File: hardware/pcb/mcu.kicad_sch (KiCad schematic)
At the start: 108 parts, among them J1 Conn_02x03_Odd_Even, J12 Conn_01x05_Pin, J3 TPS43_FPC, J6 AudioJack4, SW1 SW_PUSH, SW10 SW_PUSH, SW12 SW_PUSH, SW14 SW_PUSH, SW15 SW_PUSH, SW17 SW_PUSH, SW19 SW_PUSH, SW21 SW_PUSH, SW24 SW_PUSH, SW26 SW_PUSH, SW27 SW_PUSH, SW3 SW_PUSH, SW30 SW_PUSH, SW31 SW_PUSH, SW33 SW_PUSH, SW35 SW_PUSH, SW38 SW_PUSH, SW40 SW_PUSH, SW41 SW_PUSH, SW43 SW_PUSH, SW45 SW_PUSH, SW47 SW_PUSH, SW49 SW_PUSH, SW5 SW_PUSH, SW52 SW_PUSH, SW8 SW_PUSH, U12 SiP32431DR3, U2 D, U3 D, U6 ESP32-S3-WROOM-1, U8 NRF24L01_Breakout, U9 SRV05-4

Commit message: élagage des feuilles + réparation des tables de bibliothèques
Mae a élagué dans l'éditeur :
- mcu  : 108 -> 16 composants. Restent le S3, le nRF24, leurs découplages, le
  connecteur de prog et les 100 ohms. Partis : la matrice 26 switchs / 24
  diodes, les 11 TVS, le TRRS, l'écran, le trackpad.
- usbc : 6 -> 4 composants. Le hub CH334R (U53) est parti, il venait du coffre
  P4 et n'avait rien à faire dans une souris. Restent J48, U54 (USBLC6) et les
  deux 5k1 de CC.

Tables de bibliothèques réparées : elles pointaient vers des fichiers absents ou
renommés (optical mouse.lib -> optical_mouse.lib, nice_nano, RP2040, SSD1306).
Mouse.pretty rapatrié du fork : les 6 empreintes de la coque en dépendent.

ERC : 96 -> 24 violations.

Co-Authored-By: Claude Opus 5 <noreply@anthropic.com>
Claude-Session: https://claude.ai/code/session_01GfX5RmekmQi78Dm37qsT4Z
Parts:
- removed C5, C6: 100nF, Capacitor_SMD:C_0603_1608Metric_Pad1.08x0.95mm_HandSolder, symbol Device:C
- removed C9: 1uF, Capacitor_SMD:C_0805_2012Metric_Pad1.18x1.45mm_HandSolder, symbol Device:C
- removed D100, D101, D102, D103, D104, D105, D106, D107, D108, D109, D110: SD05C-01F, Diode_SMD:D_SOD-323, symbol Diode:SD05C-01F
- removed D11, D13, D16, D18, D2, D20, D21, D24, D26, D28, D3, D30, D32, D33, D36, D38, D40, D41, D43, D46, D48, D6, D8, D9, U2, U3: D, Diode_SMD:D_SOD-123, symbol Device:D
- removed H5, H6, H7, H8: MountingHole_Pad_MP, MountingHole:MountingHole_3.2mm_M3_DIN965_Pad, symbol Mechanical:MountingHole_Pad_MP
- removed J12: Conn_01x05_Pin, Connector_PinHeader_2.54mm:PinHeader_1x05_P2.54mm_Vertical, symbol Connector:Conn_01x05_Pin
- removed J3: TPS43_FPC, Connector_FFC-FPC:Hirose_FH12-6S-0.5SH_1x06-1MP_P0.50mm_Horizontal, symbol Connector_Generic:Conn_01x06
- removed J6: AudioJack4, EKR82-footprint:MJ-4PP-9_rev3, symbol Connector_Audio:AudioJack4
- removed R11, R14, R20, R21, R23, R25, R27, R4, R45, R47, R6, R7, R9: 100, Resistor_SMD:R_0603_1608Metric_Pad0.98x0.95mm_HandSolder, symbol Device:R
- removed R29, R32: 4.7k, Resistor_SMD:R_0603_1608Metric_Pad0.98x0.95mm_HandSolder, symbol Device:R
- removed R35, R42: 100k, Resistor_SMD:R_0603_1608Metric_Pad0.98x0.95mm_HandSolder, symbol Device:R
- removed SW1, SW10, SW12, SW14, SW15, SW17, SW19, SW21, SW24, SW26, SW27, SW3, SW30, SW31, SW33, SW35, SW38, SW40, SW41, SW43, SW45, SW47, SW49, SW5, SW52, SW8: SW_PUSH, key:SW_Cherry_MX_1.00u_PCB, symbol corne-cherry-rescue:SW_PUSH-kbd-corne-cherry-rescue
- removed U12: SiP32431DR3, Package_TO_SOT_SMD:SOT-363_SC-70-6, symbol Power_Management:SiP32431DR3
- removed U9: SRV05-4, Package_TO_SOT_SMD:SOT-23-6, symbol Power_Protection:SRV05-4
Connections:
- no-connect marks 5 -> 4

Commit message: feuille sensor + correction de mon analyse de la radio
La liaison S3 <-> nRF24 est intacte : je l'avais lue comme cassée alors que
chaque ligne passe par sa résistance série de 100 ohms, nommée localement d'un
côté (SCK_L / MOSI_L / MISO_L) et anonyme de l'autre. Rien à réparer :
  U8.5 SCK  -R30- U6.31 (GPIO38)   U8.4 CSN -R36- U6.9  (GPIO16)
  U8.6 MOSI -R18- U6.33 (GPIO40)   U8.3 CE  -R39- U6.8  (GPIO15)
  U8.7 MISO -R16- U6.32 (GPIO39)   U8.8 IRQ -R41- U6.34 (GPIO41)

Ajout de sensor.kicad_sch, cinquième feuille de la hiérarchie, avec la liste de
ce qui doit y être posé et les références exactes à respecter — SW1/SW2/SW3,
LD1/LQ1, U2 — pour que le F8 retrouve les empreintes verrouillées du PCB.

Les 20 GPIO libérés par le retrait de la matrice apparaissent maintenant en
pin_not_connected : c'est attendu, ils attendent le câblage du capteur.

Note : j'ai tenté de poser le PWR_FLAG du +5V par script, sans succès — le
symbole n'atterrissait pas sur le net. Revert. À poser dans l'éditeur.

Co-Authored-By: Claude Opus 5 <noreply@anthropic.com>
Claude-Session: https://claude.ai/code/session_01GfX5RmekmQi78Dm37qsT4Z
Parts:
- removed R49: 10k, Resistor_SMD:R_0603_1608Metric_Pad0.98x0.95mm_HandSolder, symbol Device:R
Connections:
- net CS_DPL: no longer names the net of U6.22 (GPIO14/TOUCH14/ADC2_CH3/FSPIWP/FSPIDQS/SUBSPIWP)
- net CS_P4: no longer names the net of U6.15 (GPIO3/TOUCH3/ADC1_CH2)
- net IRQ_P4: no longer names the net of U6.16 (GPIO46)
- net LINK_5V_EN: no longer names the net of U6.23 (GPIO21)
- net LINK_RX: no longer names the net of U6.11 (GPIO18/U1RXD/ADC2_CH7/CLK_OUT3)
- net LINK_TX: no longer names the net of U6.10 (GPIO17/U1TXD/ADC2_CH6)
- net TP_RDY: no longer names the net of U6.35 (MTMS/GPIO42)
- net TP_SCL: no longer names the net of U6.25 (GPIO48/SPICLK_N/SUBSPICLK_N_DIFF)
- net TP_SDA: no longer names the net of U6.24 (GPIO47/SPICLK_P/SUBSPICLK_P_DIFF)
- net col0: no longer names the net of U6.4 (GPIO4/TOUCH4/ADC1_CH3)
- net col1: no longer names the net of U6.5 (GPIO5/TOUCH5/ADC1_CH4)
- net col2: no longer names the net of U6.7 (GPIO7/TOUCH7/ADC1_CH6)
- net col3: no longer names the net of U6.17 (GPIO9/TOUCH9/ADC1_CH8/FSPIHD/SUBSPIHD)
- net col4: no longer names the net of U6.18 (GPIO10/TOUCH10/ADC1_CH9/FSPICS0/FSPIIO4/SUBSPICS0)
- net col5: no longer names the net of U6.19 (GPIO11/TOUCH11/ADC2_CH0/FSPID/FSPIIO5/SUBSPID)
- net col6: no longer names the net of U6.20 (GPIO12/TOUCH12/ADC2_CH1/FSPICLK/FSPIIO6/SUBSPICLK)
- net row0: no longer names the net of U6.39 (GPIO1/TOUCH1/ADC1_CH0)
- net row1: no longer names the net of U6.38 (GPIO2/TOUCH2/ADC1_CH1)
- net row2: no longer names the net of U6.12 (GPIO8/TOUCH8/ADC1_CH7/SUBSPICS1)
- net row3: no longer names the net of U6.6 (GPIO6/TOUCH6/ADC1_CH5)

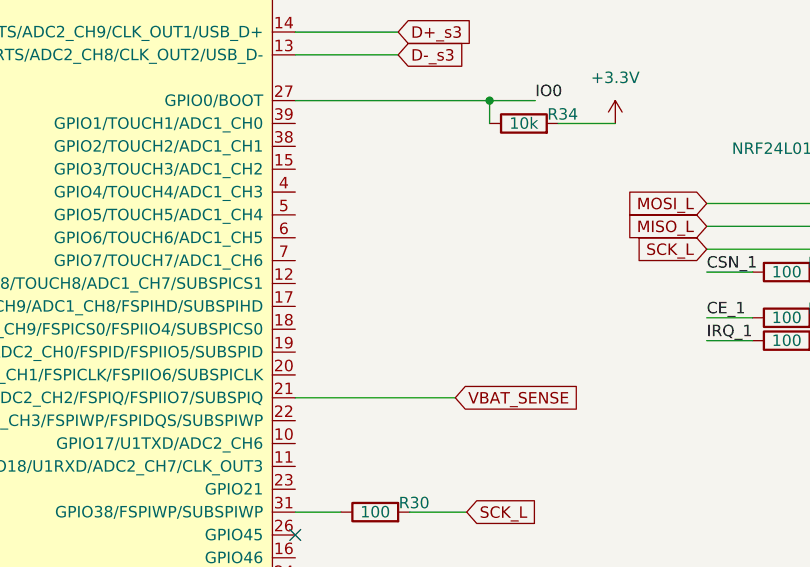
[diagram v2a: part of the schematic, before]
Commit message: schéma du capteur, de l'encodeur et des clics
sensor.kicad_sch, généré et vérifié par netlist :

- U2 PMW3360 — SPI partagé avec le nRF24 (SCK_L/MOSI_L/MISO_L, déjà routés vers
  le S3 par leurs 100 ohms), plus SNS_NCS et SNS_MOTION en propre. NRESET tiré
  au 3,3 V, LED_P pilote D100 via R101.
- U100 LDO 1,8 V dédié : VDD et VDDPIX du capteur ne sont PAS en 3,3 V (plage
  usuelle 1,8-2,1 V, à confirmer datasheet). VDDIO reste en 3,3 V.
  Découplages C100/C101 (VDD, VDDPIX), C102 (VDDIO), C103 (bulk 1,8 V).
- LD1 + R102 : LED d'illumination de la roue à 60 fentes.
  LQ1 double phototransistor, commun à la masse, voies ENC_A/ENC_B avec leurs
  pull-ups R103/R104.
- SW1/SW2/SW3 : COM à la masse, NO vers SW_LEFT/SW_RIGHT/SW_MID avec pull-ups.

Les 6 références imposées par la coque sont respectées — SW1/SW2/SW3, LD1, LQ1,
U2 — pour que le F8 retrouve les empreintes verrouillées du PCB.

Côté MCU, les 7 signaux sont accrochés sur des GPIO libérés par le clavier, en
évitant les broches de strapping et la PSRAM octale :
  GPIO4 SNS_NCS · GPIO5 SNS_MOTION · GPIO7 ENC_A · GPIO17 ENC_B
  GPIO18 SW_LEFT · GPIO19 SW_RIGHT · GPIO20 SW_MID

Deux pièges rencontrés en écrivant ces feuilles, tous deux attrapés par la
netlist : placer des fils à des coordonnées devinées ne connecte rien (il faut
calculer la position réelle des pins depuis lib_symbols), et insérer sur la
première occurrence de (embedded_fonts tombe à l'intérieur des définitions de
symboles et casse le fichier.

Co-Authored-By: Claude Opus 5 <noreply@anthropic.com>
Claude-Session: https://claude.ai/code/session_01GfX5RmekmQi78Dm37qsT4Z
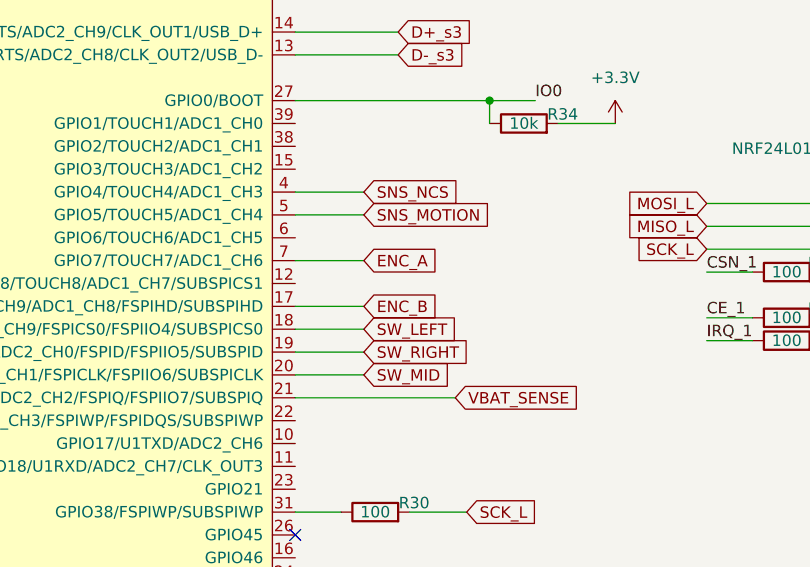
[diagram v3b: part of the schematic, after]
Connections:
- net ENC_B: now reaches U6.17 (GPIO9/TOUCH9/ADC1_CH8/FSPIHD/SUBSPIHD)
- net SW_LEFT: now reaches U6.18 (GPIO10/TOUCH10/ADC1_CH9/FSPICS0/FSPIIO4/SUBSPICS0)
- net SW_RIGHT: now reaches U6.19 (GPIO11/TOUCH11/ADC2_CH0/FSPID/FSPIIO5/SUBSPID)
- net SW_MID: now reaches U6.20 (GPIO12/TOUCH12/ADC2_CH1/FSPICLK/FSPIIO6/SUBSPICLK)
- net SNS_NCS: now reaches U6.4 (GPIO4/TOUCH4/ADC1_CH3)
- net SNS_MOTION: now reaches U6.5 (GPIO5/TOUCH5/ADC1_CH4)
- net ENC_A: now reaches U6.7 (GPIO7/TOUCH7/ADC1_CH6)
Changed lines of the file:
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@@
+		)
+	)
+	(wire
+		(pts
+			(xy 172.72 58.42) (xy 180.34 58.42)
+		)
+		(stroke
+			(width 0)
+			(type default)
+		)
+	)
+	(global_label "SNS_NCS"
+		(shape input)
+		(at 180.34 58.42 0)
+		(fields_autoplaced yes)
+		(effects
+			(font
+				(size 1.27 1.27)
+			)
+			(justify left)
+		)
+	)
+	(wire
+		(pts
+			(xy 172.72 60.96) (xy 180.34 60.96)
+		)
+		(stroke
+			(width 0)
+			(type default)
+		)
+	)
+	(global_label "SNS_MOTION"
+		(shape input)
+		(at 180.34 60.96 0)
+		(fields_autoplaced yes)
+		(effects
+			(font
+				(size 1.27 1.27)
+			)
+			(justify left)
+		)
+	)
+	(wire
+		(pts
+			(xy 172.72 66.04) (xy 180.34 66.04)
+		)
+		(stroke
+			(width 0)
+			(type default)
+		)
+	)
+	(global_label "ENC_A"
+		(shape input)
+		(at 180.34 66.04 0)
+		(fields_autoplaced yes)
+		(effects
+			(font
+				(size 1.27 1.27)
+			)
+			(justify left)
+		)
+	)
+	(wire
+		(pts
+			(xy 172.72 71.12) (xy 180.34 71.12)
+		)
+		(stroke
+			(width 0)
+			(type default)
+		)
+	)
+	(global_label "ENC_B"
+		(shape input)
+		(at 180.34 71.12 0)
+		(fields_autoplaced yes)
+		(effects
+			(font
+				(size 1.27 1.27)
+			)
+			(justify left)
+		)
+	)
+	(wire
+		(pts
+			(xy 172.72 73.66) (xy 180.34 73.66)
+		)
+		(stroke
+			(width 0)
+			(type default)
+		)
+	)
+	(global_label "SW_LEFT"
+		(shape input)
+		(at 180.34 73.66 0)
+		(fields_autoplaced yes)
+		(effects
+			(font
+				(size 1.27 1.27)
+			)
+			(justify left)
+		)
+	)
+	(wire
+		(pts
+			(xy 172.72 76.2) (xy 180.34 76.2)
+		)
+		(stroke
+			(width 0)
+			(type default)
+		)
+	)
+	(global_label "SW_RIGHT"
+		(shape input)
+		(at 180.34 76.2 0)
+		(fields_autoplaced yes)
+		(effects
+			(font
+				(size 1.27 1.27)
+			)
+			(justify left)
+		)
+	)
+	(wire
+		(pts
+			(xy 172.72 78.74) (xy 180.34 78.74)
+		)
+		(stroke
+			(width 0)
+			(type default)
+		)
+	)
+	(global_label "SW_MID"
+		(shape input)
+		(at 180.34 78.74 0)
+		(fields_autoplaced yes)
+		(effects
+			(font
+				(size 1.27 1.27)
+			)
+			(justify left)
 		)
 	)

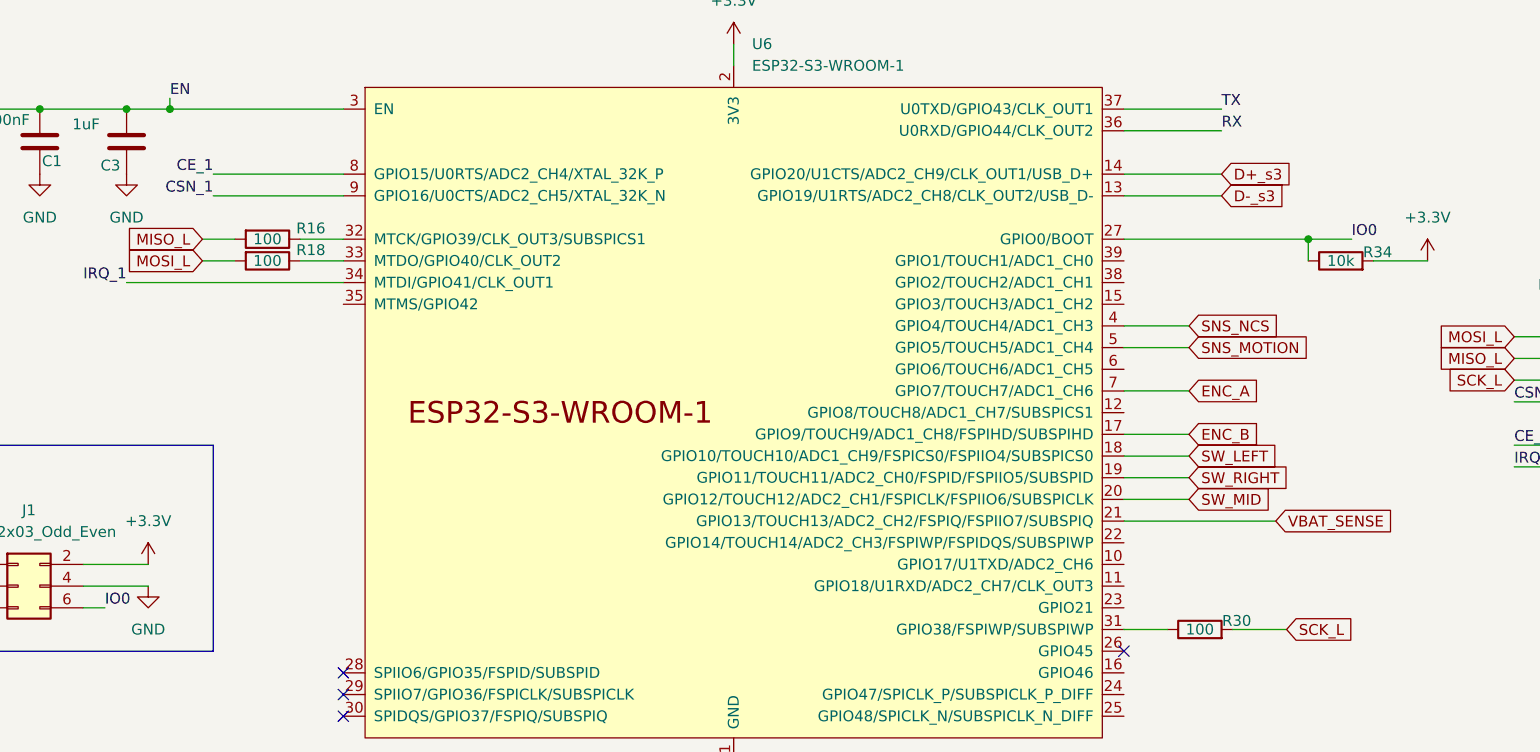
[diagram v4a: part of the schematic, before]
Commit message: contour : renflement pour le connecteur USB-C
Le J48 dépassait de 5,76 mm au-dessus du bord haut : le connecteur n'avait pas
de matière sous lui, donc pas d'USB possible. Plutôt que de le reculer — il doit
rester à l'avant, là où sortait le câble de la M100 — le contour reçoit un
renflement local : x 90,0 à 102,5, remontant de y=74,85 à y=68,5.

Le connecteur occupe x 90,98..101,62 et remonte à 69,09 : il a 0,9 mm de marge
tout autour et repose entièrement sur la carte.

Contour vérifié fermé (28 segments, zéro extrémité libre). Le PCB passe de
78 à 84,35 mm de long, la largeur reste à 39 mm — donc toujours compatible avec
les 42 mm de la zone libre du panneau Niphargus.

Piège : les coordonnées réelles étaient 81.34915 et non 81.35 (arrondi
d'affichage), et le segment était verrouillé — remplacement par parcours
balancé plutôt que par motif de texte.

Co-Authored-By: Claude Opus 5 <noreply@anthropic.com>
Claude-Session: https://claude.ai/code/session_01GfX5RmekmQi78Dm37qsT4Z
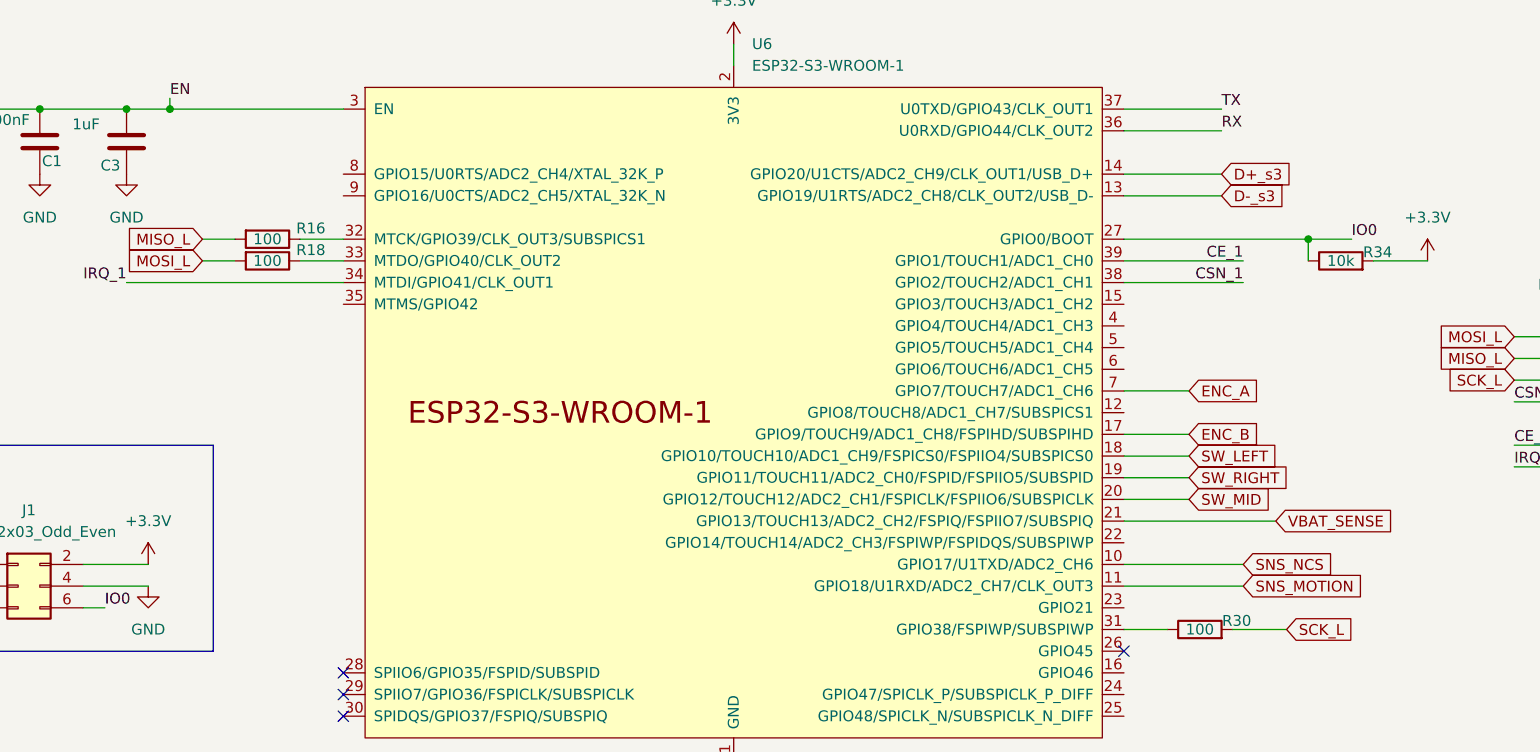
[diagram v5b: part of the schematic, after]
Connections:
- net CE_1: now also U6.39 (GPIO1/TOUCH1/ADC1_CH0); no longer U6.8 (GPIO15/U0RTS/ADC2_CH4/XTAL_32K_P)
- net CSN_1: now also U6.38 (GPIO2/TOUCH2/ADC1_CH1); no longer U6.9 (GPIO16/U0CTS/ADC2_CH5/XTAL_32K_N)
- net SNS_MOTION: now also U6.11 (GPIO18/U1RXD/ADC2_CH7/CLK_OUT3); no longer U6.5 (GPIO5/TOUCH5/ADC1_CH4)
- net SNS_NCS: now also U6.10 (GPIO17/U1TXD/ADC2_CH6); no longer U6.4 (GPIO4/TOUCH4/ADC1_CH3)
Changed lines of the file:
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@@
+	(wire
+		(pts
+			(xy 186.69 88.9) (xy 172.72 88.9)
+		)
+		(stroke
+			(width 0)
+			(type default)
+		)
+	)
+	(wire
+		(pts
+			(xy 186.69 50.8) (xy 172.72 50.8)
+		)
+		(stroke
+			(width 0)
+			(type default)
+		)
+	)
 	(wire
 		(pts
@@
 	(wire
 		(pts
-			(xy 66.04 40.64) (xy 81.28 40.64)
-		)
-		(stroke
-			(width 0)
-			(type default)
-		)
-	)
-	(wire
-		(pts
-			(xy 172.72 58.42) (xy 180.34 58.42)
-		)
-		(stroke
-			(width 0)
-			(type default)
-		)
-	)
-	(wire
-		(pts
 			(xy 55.88 53.34) (xy 81.28 53.34)
 		)
@@
 	(wire
 		(pts
+			(xy 186.69 53.34) (xy 172.72 53.34)
+		)
+		(stroke
+			(width 0)
+			(type default)
+		)
+	)
+	(wire
+		(pts
 			(xy 231.14 72.39) (xy 232.41 72.39)
 		)
@@
 	(wire
 		(pts
+			(xy 186.69 86.36) (xy 172.72 86.36)
+		)
+		(stroke
+			(width 0)
+			(type default)
+		)
+	)
+	(wire
+		(pts
 			(xy 184.15 40.64) (xy 172.72 40.64)
 		)
@@
 	(wire
 		(pts
-			(xy 66.04 43.18) (xy 81.28 43.18)
-		)
-		(stroke
-			(width 0)
-			(type default)
-		)
-	)
-	(wire
-		(pts
 			(xy 34.29 86.36) (xy 38.1 86.36)
 		)
@@
 		(pts
 			(xy 60.96 31.75) (xy 60.96 33.02)
-		)
-		(stroke
-			(width 0)
-			(type default)
-		)
-	)
-	(wire
-		(pts
-			(xy 172.72 60.96) (xy 180.34 60.96)
 		)
 		(stroke
@@
 	)
 	(label "CE_1"
-		(at 66.04 40.64 180)
+		(at 186.69 50.8 180)
 		(effects
 			(font
@@
 	)
 	(label "CSN_1"
-		(at 66.04 43.18 180)
+		(at 186.69 53.34 180)
 		(effects
 			(font
@@
 	(global_label "SNS_MOTION"
 		(shape input)
-		(at 180.34 60.96 0)
+		(at 186.69 88.9 0)
 		(fields_autoplaced yes)
 		(effects
@@
 		)
 		(property "Intersheetrefs" "${INTERSHEET_REFS}"
-			(at 180.34 60.96 0)
+			(at 186.69 88.9 0)
 			(hide yes)
 			(show_name no)
@@
 	(global_label "SNS_NCS"
 		(shape input)
-		(at 180.34 58.42 0)
+		(at 186.69 86.36 0)
 		(fields_autoplaced yes)
 		(effects
@@
 		)
 		(property "Intersheetrefs" "${INTERSHEET_REFS}"
-			(at 180.34 58.42 0)
-			(hide yes)
-			(show_name no)
+			(at 186.69 86.36 0)
+			(hide yes)
+			(show_name no)
